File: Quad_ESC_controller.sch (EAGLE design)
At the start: 26 parts, among them IC1 OP-AMP, Y1 ECS-80-S-4X

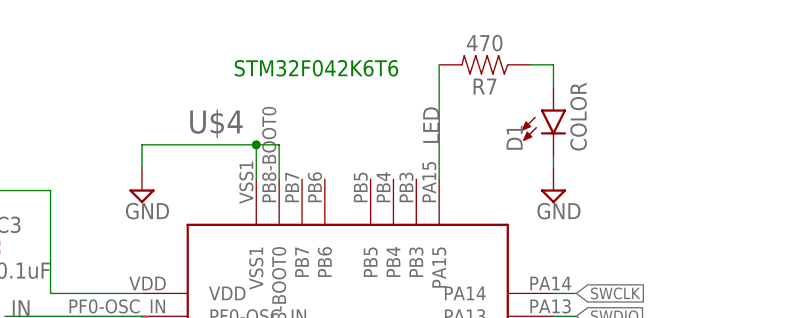
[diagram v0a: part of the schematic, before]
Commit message: Added status of chips
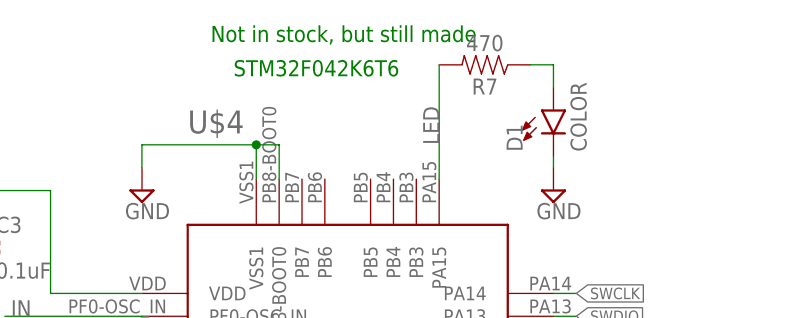
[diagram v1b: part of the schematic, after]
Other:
- note added: "Not in stock, but still made"
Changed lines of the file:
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@@
 <text x="62.23" y="50.8" size="1.778" layer="91">CAN TRANSCEIVER</text>
 <text x="50.8" y="109.22" size="1.778" layer="91">ID resistor to backplane</text>
+<text x="71.12" y="175.26" size="1.778" layer="91">Not in stock, but still made </text>
 </plain>
 <instances>

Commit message: added test points
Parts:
- added J1, J2, J3, J4, J5, J6, J7, J8: (no value), SparkFun-Connectors:CONN_01
- added OP-AMP, OP-AMP1: LM2904S, IC, LM2904:LM2904S
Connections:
- new net N$10: J1.1
- new net N$3: J4.1
- new net N$4: J5.1
- new net N$5: J6.1
- new net N$7: J7.1
- new net N$8: J3.1
- new net N$9: J2.1
- net +3V3: now also OP-AMP1P.V+, OP-AMPP.V+
- net GND: now also OP-AMP1P.V-, OP-AMPP.V-
- net N$6: now also J8.1, OP-AMP1A.IN-; no longer IC1G1.-IN
- net TLM: now also OP-AMP1A.OUT; no longer IC1G1.OUT
- net TLM_ESC: now also OP-AMP1A.IN+; no longer IC1G1.+IN

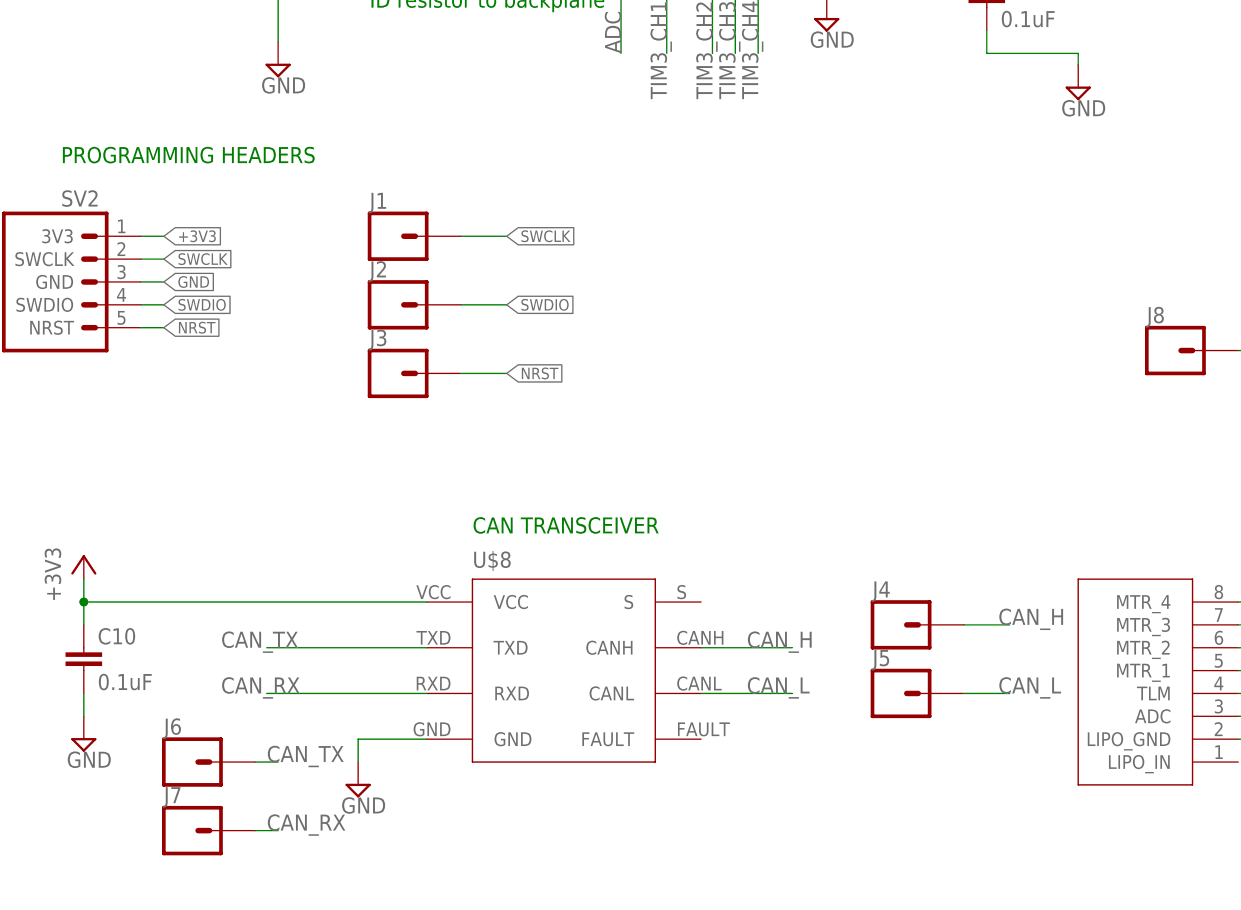
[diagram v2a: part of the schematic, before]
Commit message: made test points nice
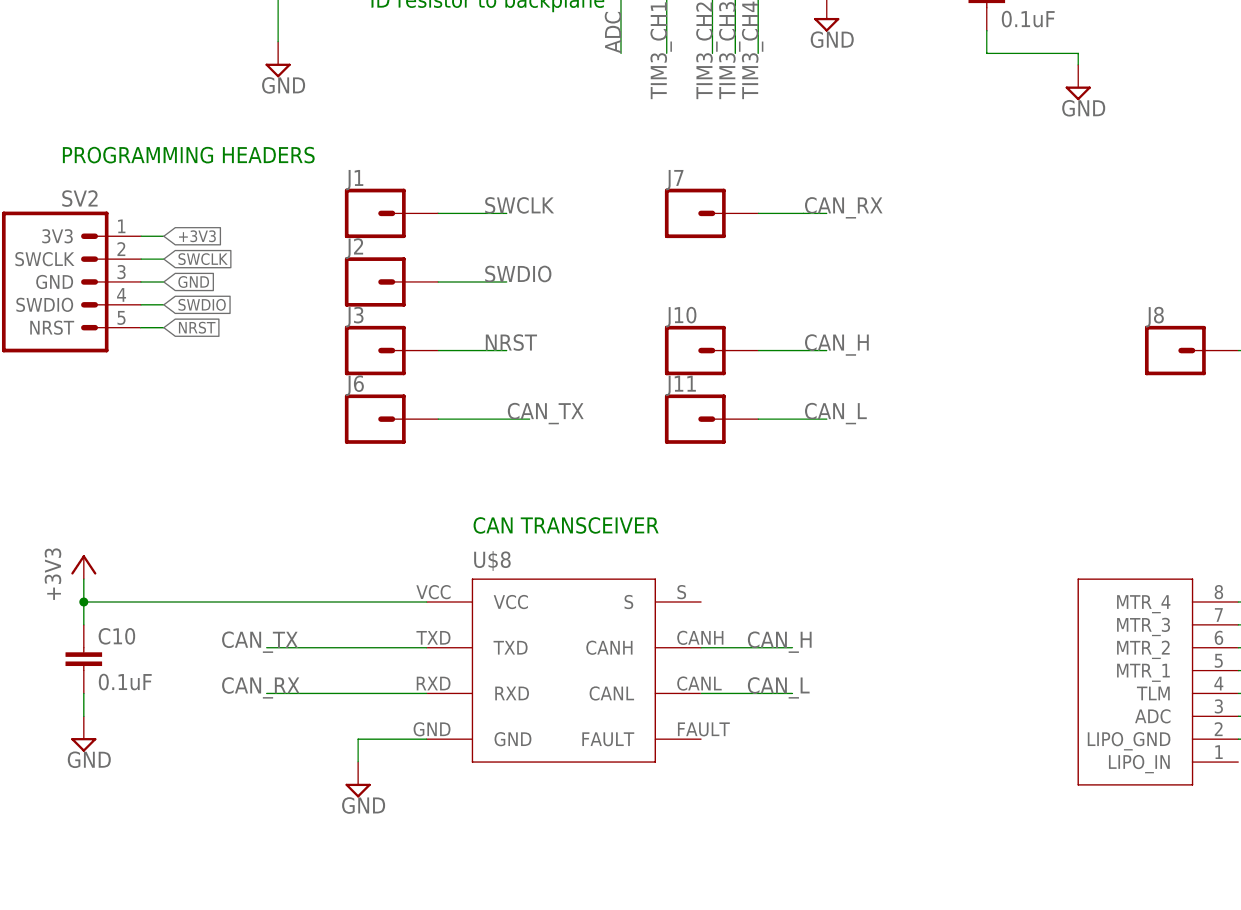
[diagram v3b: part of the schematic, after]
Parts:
- removed J4, J5: (no value), SparkFun-Connectors:CONN_01
- added J10, J11: (no value), SparkFun-Connectors:CONN_01
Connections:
- removed net N$10: J1.1
- removed net N$3: J4.1
- removed net N$4: J5.1
- removed net N$5: J6.1
- removed net N$7: J7.1
- removed net N$8: J3.1
- removed net N$9: J2.1
- net CAN_H: now also J10.1
- net CAN_L: now also J11.1
- net CAN_RX: now also J7.1
- net CAN_TX: now also J6.1
- net NRST: now also J3.1
- net SWCLK: now also J1.1
- net SWDIO: now also J2.1
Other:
- moved on the sheet: J1, J2, J3, J6, J7

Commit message: check this
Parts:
- removed J1, J10, J11, J2, J3, J6, J8: (no value), SparkFun-Connectors:CONN_01
- removed OP-AMP, OP-AMP1: LM2904S, IC, LM2904:LM2904S
- J7: device SparkFun-Connectors:CONN_01 -> SparkFun-Connectors:CONN_06SILK_FEMALE_PTH
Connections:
- net +3V3: no longer OP-AMP1P.V+, OP-AMPP.V+
- net ADC: now also J7.1
- net CAN_H: no longer J10.1
- net CAN_L: no longer J11.1
- net CAN_RX: no longer J7.1
- net CAN_TX: no longer J6.1
- net GND: no longer OP-AMP1P.V-, OP-AMPP.V-
- net N$6: now also IC1G1.-IN; no longer J8.1, OP-AMP1A.IN-
- net NRST: no longer J3.1
- net SWCLK: no longer J1.1
- net SWDIO: no longer J2.1
- net TIM3_CH1: now also J7.3
- net TIM3_CH2: now also J7.4
- net TIM3_CH3: now also J7.5
- net TIM3_CH4: now also J7.6
- net TLM: now also IC1G1.OUT; no longer OP-AMP1A.OUT
- net TLM_ESC: now also IC1G1.+IN, J7.2; no longer OP-AMP1A.IN+
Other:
- note added: "ALL ONE OP-AMP - LM358"
- note added: "Test points"
- note removed: "Not in stock, but still made"
